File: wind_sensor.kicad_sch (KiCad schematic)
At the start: 13 parts, among them J1 Conn_01x08_Male, J2 Conn_01x08_Male, U1 AS5600, U2 MAX40200AUK

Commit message: remove regulator
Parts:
- removed R5: 10k, Resistor_THT:R_Array_SIP4, symbol Device:R
- removed U2: MAX40200AUK, Package_TO_SOT_SMD:SOT-23-5, symbol Analog_Switch:MAX40200AUK
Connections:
- net 3.3V is gone; now on net VCC: J1.2 (Pin_2)
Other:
- note removed: "for some reason both 3.3 and 5 are feed"
- note removed: "regulator"
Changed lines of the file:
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@@
     (rev "v01")
   )
-  (junction (at 206.375 107.95) (diameter 0) (color 0 0 0 0)
-  )
   (junction (at 259.08 79.375) (diameter 0) (color 0 0 0 0)
   )
@@
     (stroke (width 0) (type default) (color 0 0 0 0))
   )
-  (wire (pts (xy 221.615 113.03) (xy 221.615 115.57))
-    (stroke (width 0) (type default) (color 0 0 0 0))
-  )
   (wire (pts (xy 228.6 64.77) (xy 228.6 68.58))
     (stroke (width 0) (type default) (color 0 0 0 0))
@@
     (stroke (width 0) (type default) (color 0 0 0 0))
   )
+  (wire (pts (xy 158.75 74.93) (xy 161.29 74.93))
+    (stroke (width 0) (type default) (color 0 0 0 0))
+  )
   (wire (pts (xy 259.08 79.375) (xy 260.985 79.375))
     (stroke (width 0) (type default) (color 0 0 0 0))
   )
-  (wire (pts (xy 206.375 107.95) (xy 211.455 107.95))
-    (stroke (width 0) (type default) (color 0 0 0 0))
-  )
   (wire (pts (xy 227.965 64.77) (xy 228.6 64.77))
     (stroke (width 0) (type default) (color 0 0 0 0))
@@
     (stroke (width 0) (type default) (color 0 0 0 0))
   )
-  (wire (pts (xy 200.66 107.95) (xy 206.375 107.95))
-    (stroke (width 0) (type default) (color 0 0 0 0))
-  )
-  (wire (pts (xy 206.375 107.95) (xy 206.375 110.49))
-    (stroke (width 0) (type default) (color 0 0 0 0))
-  )
   (wire (pts (xy 114.935 80.01) (xy 118.11 80.01))
     (stroke (width 0) (type default) (color 0 0 0 0))
@@
     (effects (font (size 1.27 1.27)) (justify left bottom))
   )
-  (text "regulator" (at 198.12 94.615 0)
-    (effects (font (size 3 3)) (justify left bottom))
-  )
   (text "voltage selector" (at 160.655 71.12 0)
     (effects (font (size 1.27 1.27)) (justify left bottom))
@@
   )
   (text "opt resistor = power resistor" (at 220.98 50.165 0)
-    (effects (font (size 1.27 1.27)) (justify left bottom))
-  )
-  (text "for some reason both 3.3 and 5 are feed" (at 234.315 99.695 0)
     (effects (font (size 1.27 1.27)) (justify left bottom))
   )
@@
     (effects (font (size 1.27 1.27)) (justify left bottom))
   )
-  (label "VDD" (at 231.775 102.87 0)
-    (effects (font (size 1.27 1.27)) (justify left bottom))
-  )
   (label "TX" (at 138.43 80.01 0)
     (effects (font (size 1.27 1.27)) (justify left bottom))
   )
-  (label "5V" (at 161.29 81.915 0)
-    (effects (font (size 1.27 1.27)) (justify left bottom))
-  )
   (label "INT" (at 138.43 77.47 0)
-    (effects (font (size 1.27 1.27)) (justify left bottom))
-  )
-  (label "CS" (at 200.66 107.95 0)
     (effects (font (size 1.27 1.27)) (justify left bottom))
   )
@@
     (effects (font (size 1.27 1.27)) (justify left bottom))
   )
-  (global_label "VCC" (shape input) (at 161.29 77.47 0) (fields_autoplaced)
-    (effects (font (size 1.27 1.27)) (justify left))
-    (property "Intersheet References" "${INTERSHEET_REFS}" (id 0) (at 167.3317 77.3906 0)
-      (effects (font (size 1.27 1.27)) (justify left) hide)
+  (global_label "VCC" (shape input) (at 158.75 74.93 180) (fields_autoplaced)
+    (effects (font (size 1.27 1.27)) (justify right))
+    (property "Intersheet References" "${INTERSHEET_REFS}" (id 0) (at 152.7083 75.0094 0)
+      (effects (font (size 1.27 1.27)) (justify right) hide)
     )
   )
@@
     (property "Intersheet References" "${INTERSHEET_REFS}" (id 0) (at 199.3106 55.5533 90)
       (effects (font (size 1.27 1.27)) (justify left) hide)
-    )
-  )
-  (global_label "VCC" (shape input) (at 211.455 102.87 180) (fields_autoplaced)
-    (effects (font (size 1.27 1.27)) (justify right))
-    (property "Intersheet References" "${INTERSHEET_REFS}" (id 0) (at 205.4133 102.9494 0)
-      (effects (font (size 1.27 1.27)) (justify right) hide)
     )
   )
@@
     (pin "8")
   )
-  (symbol (lib_id "Device:R") (at 206.375 114.3 0) (unit 1)
-    (in_bom yes) (on_board yes)
-    (property "Reference" "R5" (id 0) (at 208.28 113.0299 0)
-      (effects (font (size 1.27 1.27)) (justify left))
-    )
-    (property "Value" "10k" (id 1) (at 208.28 115.5699 90)
-      (effects (font (size 1.27 1.27)) (justify left))
-    )
-    (property "Footprint" "Resistor_THT:R_Array_SIP4" (id 2) (at 204.597 114.3 90)
-      (effects (font (size 1.27 1.27)) hide)
-    )
-    (property "Datasheet" "~" (id 3) (at 206.375 114.3 0)
-      (effects (font (size 1.27 1.27)) hide)
-    )
-    (pin "1")
-    (pin "2")
-  )
   (symbol (lib_id "power:GND") (at 160.02 111.125 90) (unit 1)
     (in_bom yes) (on_board yes) (fields_autoplaced)
@@
     (pin "2")
   )
-  (symbol (lib_id "power:GND") (at 221.615 115.57 0) (unit 1)
-    (in_bom yes) (on_board yes) (fields_autoplaced)
-    (property "Reference" "#PWR0108" (id 0) (at 221.615 121.92 0)
-      (effects (font (size 1.27 1.27)) hide)
-    )
-    (property "Value" "GND" (id 1) (at 221.615 120.65 0))
-    (property "Footprint" "" (id 2) (at 221.615 115.57 0)
-      (effects (font (size 1.27 1.27)) hide)
-    )
-    (property "Datasheet" "" (id 3) (at 221.615 115.57 0)
-      (effects (font (size 1.27 1.27)) hide)
-    )
-    (pin "1")
-  )
   (symbol (lib_id "Device:R") (at 215.9 66.675 0) (unit 1)
     (in_bom yes) (on_board yes) (fields_autoplaced)
@@
     (pin "1")
     (pin "2")
-  )
-  (symbol (lib_id "power:GND") (at 206.375 118.11 0) (unit 1)
-    (in_bom yes) (on_board yes) (fields_autoplaced)
-    (property "Reference" "#PWR0109" (id 0) (at 206.375 124.46 0)
-      (effects (font (size 1.27 1.27)) hide)
-    )
-    (property "Value" "GND" (id 1) (at 206.375 123.19 0))
-    (property "Footprint" "" (id 2) (at 206.375 118.11 0)
-      (effects (font (size 1.27 1.27)) hide)
-    )
-    (property "Datasheet" "" (id 3) (at 206.375 118.11 0)
-      (effects (font (size 1.27 1.27)) hide)
-    )
-    (pin "1")
   )
   (symbol (lib_id "power:GND") (at 113.03 100.33 0) (unit 1)
@@
     (pin "2")
   )
-  (symbol (lib_id "Analog_Switch:MAX40200AUK") (at 221.615 105.41 0) (unit 1)
-    (in_bom yes) (on_board yes) (fields_autoplaced)
-    (property "Reference" "U2" (id 0) (at 221.615 95.25 0))
-    (property "Value" "MAX40200AUK" (id 1) (at 221.615 97.79 0))
-    (property "Footprint" "Package_TO_SOT_SMD:SOT-23-5" (id 2) (at 221.615 92.71 0)
-      (effects (font (size 1.27 1.27)) hide)
-    )
-    (property "Datasheet" "https://datasheets.maximintegrated.com/en/ds/MAX40200.pdf" (id 3) (at 221.615 92.71 0)
-      (effects (font (size 1.27 1.27)) hide)
-    )
-    (pin "1")
-    (pin "2")
-    (pin "3")
-    (pin "4")
-    (pin "5")
-  )
   (symbol (lib_id "Device:C") (at 269.875 83.185 0) (unit 1)
     (in_bom yes) (on_board yes) (fields_autoplaced)
@@
       (reference "#PWR0107") (unit 1) (value "GND") (footprint "")
     )
-    (path "/51a726a4-caa3-4bc1-abe9-f042265e4f56"
-      (reference "#PWR0108") (unit 1) (value "GND") (footprint "")
-    )
-    (path "/57c92b67-101f-46d8-9e1b-819e76faa10d"
-      (reference "#PWR0109") (unit 1) (value "GND") (footprint "")
-    )
     (path "/214ec33d-32cf-41e8-b646-96cb76be4105"
       (reference "#PWR0110") (unit 1) (value "GND") (footprint "")
@@
       (reference "R4") (unit 1) (value "OPT") (footprint "Resistor_THT:R_Axial_DIN0207_L6.3mm_D2.5mm_P2.54mm_Vertical")
     )
-    (path "/1016685b-d600-4f5b-a189-2e43efb90f5c"
-      (reference "R5") (unit 1) (value "10k") (footprint "Resistor_THT:R_Array_SIP4")
-    )
     (path "/29f7e56b-7452-4c83-a044-bddf3364cd55"
       (reference "R6") (unit 1) (value "0") (footprint "Resistor_THT:R_Axial_DIN0204_L3.6mm_D1.6mm_P1.90mm_Vertical")
@@
       (reference "U1") (unit 1) (value "AS5600") (footprint "AS5600:AS5600L-ASOM_AMS")
     )
-    (path "/abe6c063-04e8-442a-a1b1-a5d67e64a60a"
-      (reference "U2") (unit 1) (value "MAX40200AUK") (footprint "Package_TO_SOT_SMD:SOT-23-5")
-    )
-  )
+  )

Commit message: add another led in schematic
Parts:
- added LD2: LED, LED_SMD:LED-APA102-2020, symbol Device:LED
- added R10: 470, Resistor_THT:R_Axial_DIN0207_L6.3mm_D2.5mm_P2.54mm_Vertical, symbol Device:R
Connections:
- net GND: now also LD2.1 (K)
- net VCC: now also C2.1, R6.1, U1.1 (VDD_5V), R10.1
- net VDD: no longer C2.1, R6.1, U1.1 (VDD_5V)
- new net: LD2.2 (A), R10.2
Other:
- note added: "330 resistor before the pwm led"
- moved on the sheet: J1, J2, LD1, R1

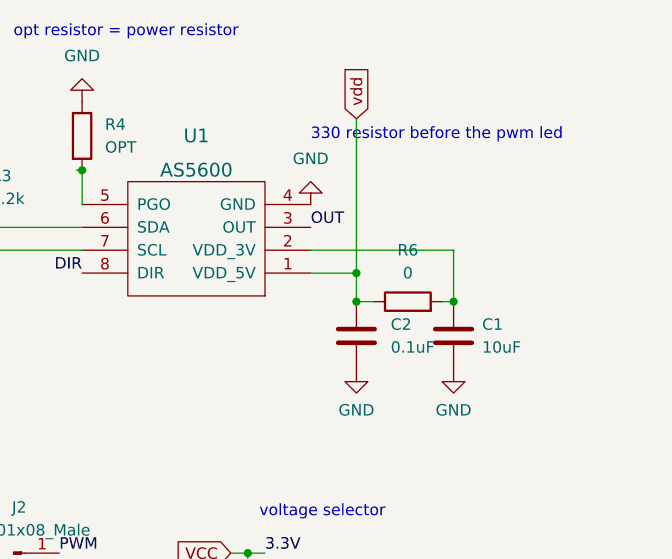
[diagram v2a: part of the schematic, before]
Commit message: replace 0 ohm ressistor with direct connection
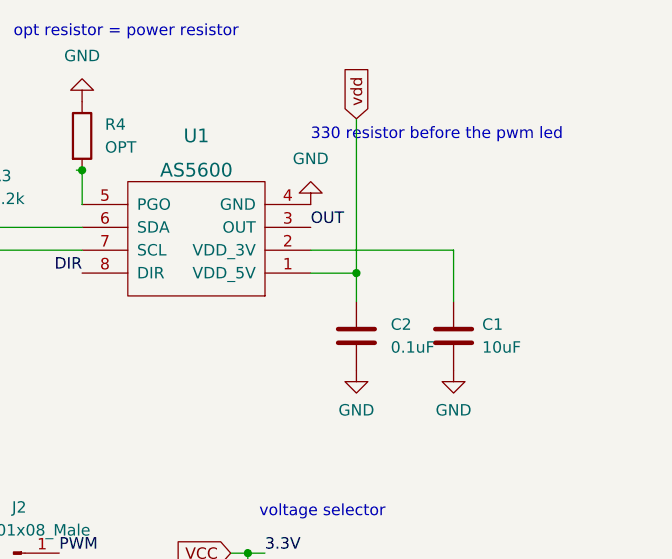
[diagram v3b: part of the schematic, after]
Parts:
- removed R6: 0, Resistor_THT:R_Axial_DIN0204_L3.6mm_D1.6mm_P1.90mm_Vertical, symbol Device:R
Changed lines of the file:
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@@
     (rev "v01")
   )
-  (junction (at 259.08 79.375) (diameter 0) (color 0 0 0 0)
-  )
   (junction (at 215.9 71.12) (diameter 0) (color 0 0 0 0)
   )
@@
   (junction (at 259.08 76.2) (diameter 0) (color 0 0 0 0)
   )
-  (junction (at 269.875 79.375) (diameter 0) (color 0 0 0 0)
-  )
   (wire (pts (xy 215.9 60.96) (xy 215.9 62.865))
     (stroke (width 0) (type default) (color 0 0 0 0))
@@
     (stroke (width 0) (type default) (color 0 0 0 0))
   )
-  (wire (pts (xy 259.08 79.375) (xy 260.985 79.375))
-    (stroke (width 0) (type default) (color 0 0 0 0))
-  )
   (wire (pts (xy 227.965 64.77) (xy 228.6 64.77))
     (stroke (width 0) (type default) (color 0 0 0 0))
@@
   )
   (wire (pts (xy 226.06 125.095) (xy 233.045 125.095))
-    (stroke (width 0) (type default) (color 0 0 0 0))
-  )
-  (wire (pts (xy 268.605 79.375) (xy 269.875 79.375))
     (stroke (width 0) (type default) (color 0 0 0 0))
   )
@@
     (pin "1")
   )
-  (symbol (lib_id "Device:R") (at 264.795 79.375 90) (unit 1)
-    (in_bom yes) (on_board yes) (fields_autoplaced)
-    (property "Reference" "R6" (id 0) (at 264.795 73.66 90))
-    (property "Value" "0" (id 1) (at 264.795 76.2 90))
-    (property "Footprint" "Resistor_THT:R_Axial_DIN0204_L3.6mm_D1.6mm_P1.90mm_Vertical" (id 2) (at 264.795 81.153 90)
-      (effects (font (size 1.27 1.27)) hide)
-    )
-    (property "Datasheet" "~" (id 3) (at 264.795 79.375 0)
-      (effects (font (size 1.27 1.27)) hide)
-    )
-    (pin "1")
-    (pin "2")
-  )
   (symbol (lib_id "Device:R") (at 228.6 60.96 0) (unit 1)
     (in_bom yes) (on_board yes)
@@
       (reference "R4") (unit 1) (value "OPT") (footprint "Resistor_THT:R_Axial_DIN0207_L6.3mm_D2.5mm_P2.54mm_Vertical")
     )
-    (path "/29f7e56b-7452-4c83-a044-bddf3364cd55"
-      (reference "R6") (unit 1) (value "0") (footprint "Resistor_THT:R_Axial_DIN0204_L3.6mm_D1.6mm_P1.90mm_Vertical")
-    )
     (path "/567b4484-7d7f-4e48-993a-4d02d9191135"
